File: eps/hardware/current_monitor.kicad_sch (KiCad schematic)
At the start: 23 parts, among them Q5 IRLML0030, Q6 IRLML0030, U5 NCS214RSQT2G, U6 74LVC1G07SE-7

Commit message: start footprint assignment
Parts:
- C22, C23, C24, C25, C26, C27, C28, C29: footprint (none) -> Capacitor_SMD:C_0603_1608Metric
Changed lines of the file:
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@@
 			)
 		)
-		(property "Footprint" ""
+		(property "Footprint" "Capacitor_SMD:C_0603_1608Metric"
 			(at 261.62 58.42 0)
 			(effects
@@
 			)
 		)
-		(property "Footprint" ""
+		(property "Footprint" "Capacitor_SMD:C_0603_1608Metric"
 			(at 127 100.33 0)
 			(effects
@@
 			)
 		)
-		(property "Footprint" ""
+		(property "Footprint" "Capacitor_SMD:C_0603_1608Metric"
 			(at 208.28 58.42 0)
 			(effects
@@
 			)
 		)
-		(property "Footprint" ""
+		(property "Footprint" "Capacitor_SMD:C_0603_1608Metric"
 			(at 106.68 59.69 0)
 			(effects
@@
 			)
 		)
-		(property "Footprint" ""
+		(property "Footprint" "Capacitor_SMD:C_0603_1608Metric"
 			(at 157.48 135.89 0)
 			(effects
@@
 			)
 		)
-		(property "Footprint" ""
+		(property "Footprint" "Capacitor_SMD:C_0603_1608Metric"
 			(at 38.1 123.19 0)
 			(effects
@@
 			)
 		)
-		(property "Footprint" ""
+		(property "Footprint" "Capacitor_SMD:C_0603_1608Metric"
 			(at 102.87 135.89 0)
 			(effects
@@
 			)
 		)
-		(property "Footprint" ""
+		(property "Footprint" "Capacitor_SMD:C_0603_1608Metric"
 			(at 250.19 69.85 0)
 			(effects

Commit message: finish footprint assignment and board setup
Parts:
- NT1: footprint (none) -> NetTie:NetTie-2_SMD_Pad0.5mm
- R24, R25, R26, R27, R28, R29, R30, R31: footprint (none) -> Resistor_SMD:R_0603_1608Metric
- U5: footprint (none) -> Package_TO_SOT_SMD:SOT-363_SC-70-6
- U6: footprint (none) -> Package_TO_SOT_SMD:SOT-353_SC-70-5
- U7: footprint (none) -> Package_TO_SOT_SMD:SOT-23-6
- U8: footprint (none) -> Package_SON:WSON-6-1EP_2x2mm_P0.65mm_EP1x1.6mm
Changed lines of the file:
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@@
 			)
 		)
-		(property "Footprint" ""
+		(property "Footprint" "Resistor_SMD:R_0603_1608Metric"
 			(at 49.276 52.324 90)
 			(effects
@@
 			)
 		)
-		(property "Footprint" ""
+		(property "Footprint" "Resistor_SMD:R_0603_1608Metric"
 			(at 176.276 67.564 90)
 			(effects
@@
 			)
 		)
-		(property "Footprint" ""
+		(property "Footprint" "Resistor_SMD:R_0603_1608Metric"
 			(at 255.016 45.974 90)
 			(effects
@@
 			)
 		)
-		(property "Footprint" ""
+		(property "Footprint" "Package_TO_SOT_SMD:SOT-353_SC-70-5"
 			(at 91.44 73.66 0)
 			(effects
@@
 			)
 		)
-		(property "Footprint" ""
+		(property "Footprint" "Package_SON:WSON-6-1EP_2x2mm_P0.65mm_EP1x1.6mm"
 			(at 232.41 55.88 0)
 			(effects
@@
 			)
 		)
-		(property "Footprint" ""
+		(property "Footprint" "Package_TO_SOT_SMD:SOT-363_SC-70-6"
 			(at 71.12 118.11 0)
 			(effects
@@
 			)
 		)
-		(property "Footprint" ""
+		(property "Footprint" "Resistor_SMD:R_0603_1608Metric"
 			(at 194.056 67.564 90)
 			(effects
@@
 			)
 		)
-		(property "Footprint" ""
+		(property "Footprint" "Resistor_SMD:R_0603_1608Metric"
 			(at 117.856 136.144 90)
 			(effects
@@
 			)
 		)
-		(property "Footprint" ""
+		(property "Footprint" "Resistor_SMD:R_0603_1608Metric"
 			(at 163.576 67.564 90)
 			(effects
@@
 			)
 		)
-		(property "Footprint" ""
+		(property "Footprint" "NetTie:NetTie-2_SMD_Pad0.5mm"
 			(at 57.15 41.91 0)
 			(effects
@@
 			)
 		)
-		(property "Footprint" ""
+		(property "Footprint" "Resistor_SMD:R_0603_1608Metric"
 			(at 213.106 33.274 90)
 			(effects
@@
 			)
 		)
-		(property "Footprint" ""
+		(property "Footprint" "Package_TO_SOT_SMD:SOT-23-6"
 			(at 139.7 116.84 0)
 			(effects
@@
 			)
 		)
-		(property "Footprint" ""
+		(property "Footprint" "Resistor_SMD:R_0603_1608Metric"
 			(at 250.444 91.694 90)
 			(effects

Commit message: fix update errors
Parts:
- U8: value ~ -> TPS22810DRVT
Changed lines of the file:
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@@
 			)
 		)
-		(property "Value" "~"
+		(property "Value" "TPS22810DRVT"
 			(at 232.41 38.1 0)
 			(effects
@@
 		(pin "2"
 		)
+		(pin "7"
+		)
 		(instances

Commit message: schematic fixes
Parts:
- C22, C23, C24, C25, C26, C27, C28, C29: footprint Capacitor_SMD:C_0603_1608Metric -> Capacitor_SMD:C_0402_1005Metric
- R24, R25, R26, R27, R28, R29, R30, R31: footprint Resistor_SMD:R_0603_1608Metric -> Resistor_SMD:R_0402_1005Metric
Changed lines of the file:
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@@
 			)
 		)
-		(property "Footprint" "Resistor_SMD:R_0603_1608Metric"
+		(property "Footprint" "Resistor_SMD:R_0402_1005Metric"
 			(at 49.276 52.324 90)
 			(effects
@@
 			)
 		)
-		(property "Footprint" "Resistor_SMD:R_0603_1608Metric"
+		(property "Footprint" "Resistor_SMD:R_0402_1005Metric"
 			(at 176.276 67.564 90)
 			(effects
@@
 			)
 		)
-		(property "Footprint" "Capacitor_SMD:C_0603_1608Metric"
+		(property "Footprint" "Capacitor_SMD:C_0402_1005Metric"
 			(at 261.62 58.42 0)
 			(effects
@@
 			)
 		)
-		(property "Footprint" "Capacitor_SMD:C_0603_1608Metric"
+		(property "Footprint" "Capacitor_SMD:C_0402_1005Metric"
 			(at 127 100.33 0)
 			(effects
@@
 			)
 		)
-		(property "Footprint" "Resistor_SMD:R_0603_1608Metric"
+		(property "Footprint" "Resistor_SMD:R_0402_1005Metric"
 			(at 255.016 45.974 90)
 			(effects
@@
 			)
 		)
-		(property "Footprint" "Capacitor_SMD:C_0603_1608Metric"
+		(property "Footprint" "Capacitor_SMD:C_0402_1005Metric"
 			(at 208.28 58.42 0)
 			(effects
@@
 			)
 		)
-		(property "Footprint" "Capacitor_SMD:C_0603_1608Metric"
+		(property "Footprint" "Capacitor_SMD:C_0402_1005Metric"
 			(at 106.68 59.69 0)
 			(effects
@@
 			)
 		)
-		(property "Footprint" "Resistor_SMD:R_0603_1608Metric"
+		(property "Footprint" "Resistor_SMD:R_0402_1005Metric"
 			(at 194.056 67.564 90)
 			(effects
@@
 			)
 		)
-		(property "Footprint" "Resistor_SMD:R_0603_1608Metric"
+		(property "Footprint" "Resistor_SMD:R_0402_1005Metric"
 			(at 117.856 136.144 90)
 			(effects
@@
 			)
 		)
-		(property "Footprint" "Resistor_SMD:R_0603_1608Metric"
+		(property "Footprint" "Resistor_SMD:R_0402_1005Metric"
 			(at 163.576 67.564 90)
 			(effects
@@
 			)
 		)
-		(property "Footprint" "Capacitor_SMD:C_0603_1608Metric"
+		(property "Footprint" "Capacitor_SMD:C_0402_1005Metric"
 			(at 157.48 135.89 0)
 			(effects
@@
 			)
 		)
-		(property "Footprint" "Capacitor_SMD:C_0603_1608Metric"
+		(property "Footprint" "Capacitor_SMD:C_0402_1005Metric"
 			(at 38.1 123.19 0)
 			(effects
@@
 			)
 		)
-		(property "Footprint" "Capacitor_SMD:C_0603_1608Metric"
+		(property "Footprint" "Capacitor_SMD:C_0402_1005Metric"
 			(at 102.87 135.89 0)
 			(effects
@@
 			)
 		)
-		(property "Footprint" "Capacitor_SMD:C_0603_1608Metric"
+		(property "Footprint" "Capacitor_SMD:C_0402_1005Metric"
 			(at 250.19 69.85 0)
 			(effects
@@
 			)
 		)
-		(property "Footprint" "Resistor_SMD:R_0603_1608Metric"
+		(property "Footprint" "Resistor_SMD:R_0402_1005Metric"
 			(at 213.106 33.274 90)
 			(effects
@@
 			)
 		)
-		(property "Footprint" "Resistor_SMD:R_0603_1608Metric"
+		(property "Footprint" "Resistor_SMD:R_0402_1005Metric"
 			(at 250.444 91.694 90)
 			(effects

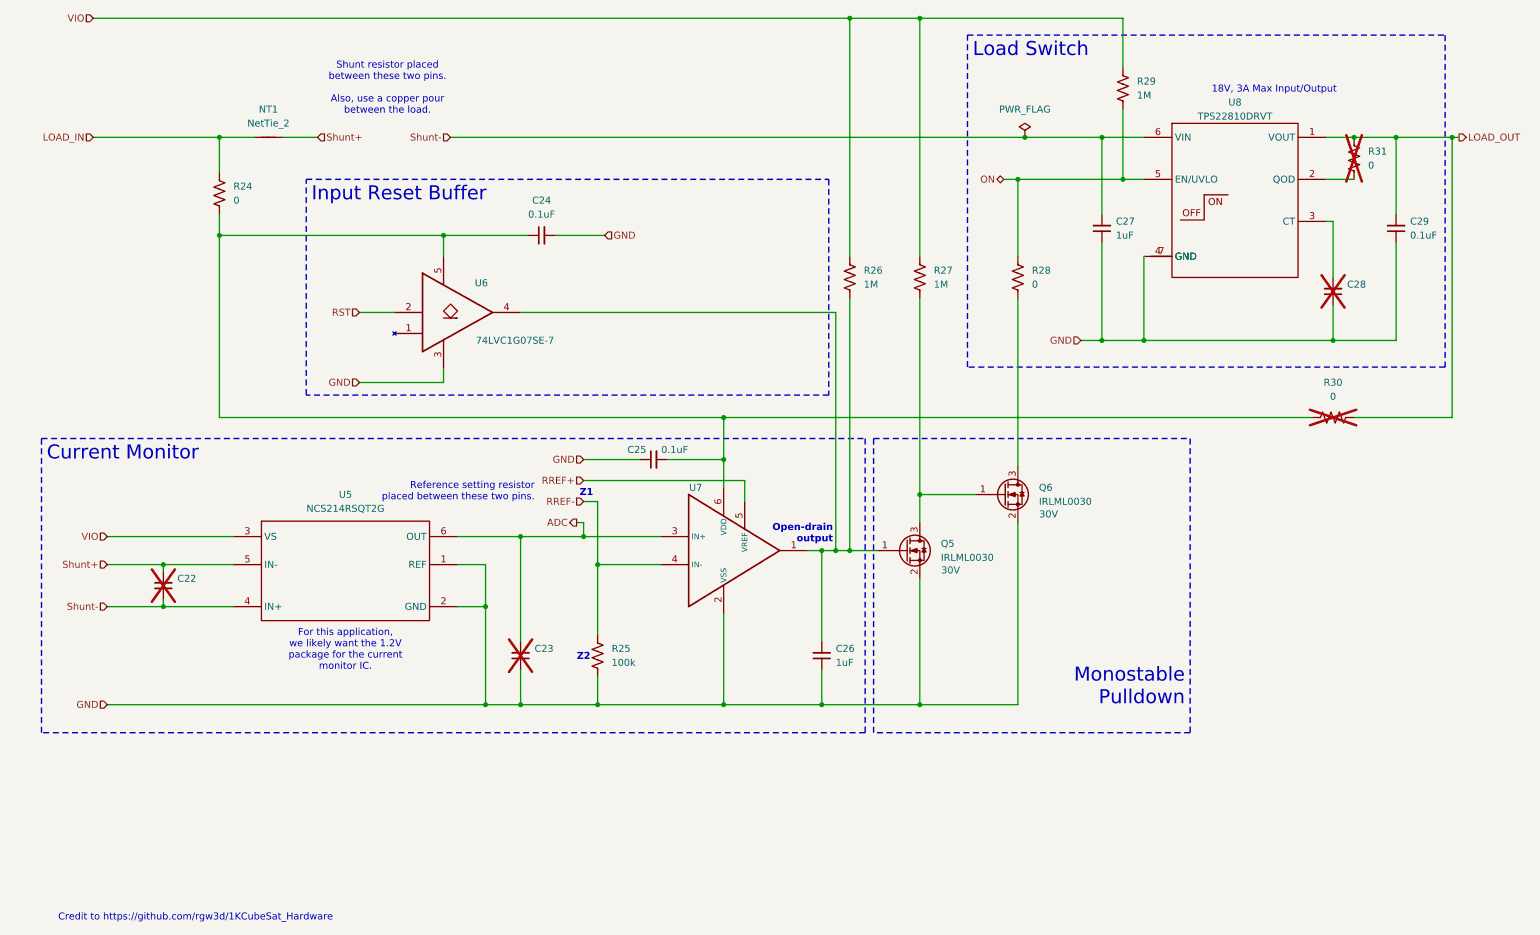
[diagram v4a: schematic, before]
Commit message: start placement of one current monitor
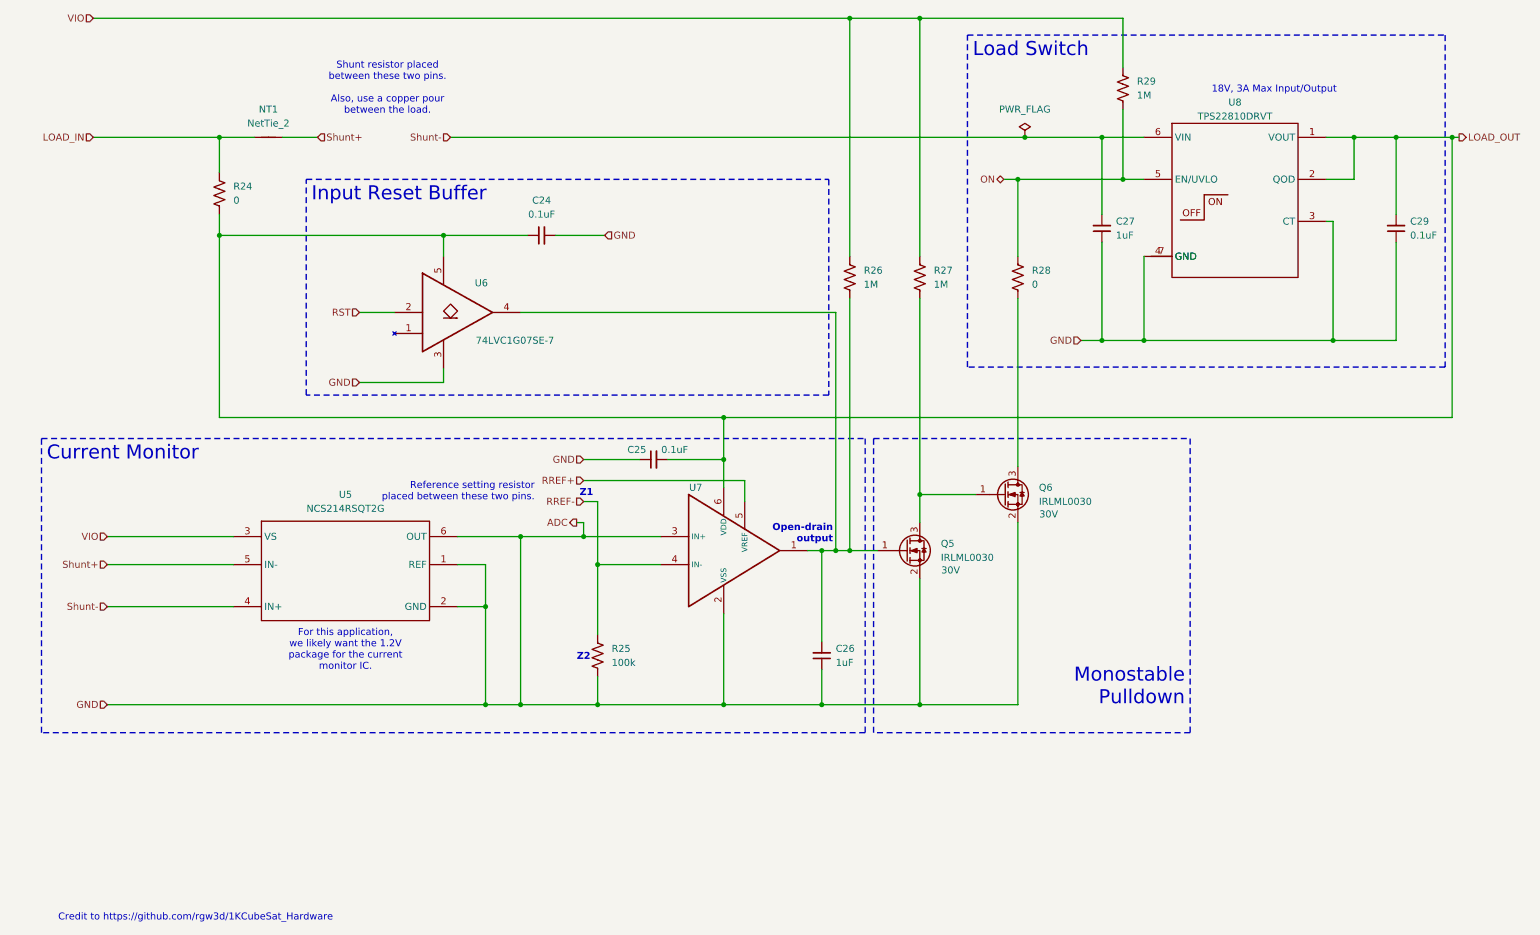
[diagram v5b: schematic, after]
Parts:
- removed C22, C23, C28: ~, Capacitor_SMD:C_0402_1005Metric, symbol Device:C_Small
- removed R30, R31: 0, Resistor_SMD:R_0402_1005Metric, symbol Device:R_US
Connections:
- net GND is gone; now on net ADC: C24.2, C25.1, C26.1, C27.1, C29.1, Q5.2 (S), Q6.2 (S), R25.2, U5.1 (REF), U5.2 (GND), U6.3, U7.2 (VSS), U8.4 (GND)
- net ADC: now also U8.3 (CT)
- net LOAD_OUT: now also C24.1, C25.2, R24.2, U6.5, U7.6 (VDD), U8.2 (QOD)

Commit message: add better current monitoring layout
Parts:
- C27: footprint Capacitor_SMD:C_0402_1005Metric -> Capacitor_SMD:C_0805_2012Metric
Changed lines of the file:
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@@
 			)
 		)
-		(property "Footprint" "Capacitor_SMD:C_0402_1005Metric"
+		(property "Footprint" "Capacitor_SMD:C_0805_2012Metric"
 			(at 208.28 58.42 0)
 			(effects

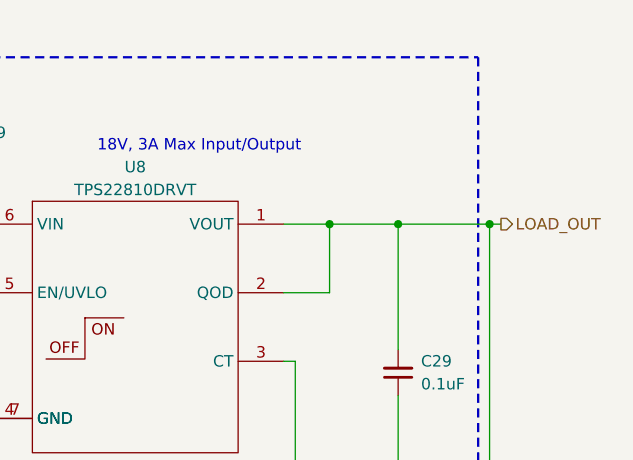
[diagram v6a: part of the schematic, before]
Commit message: finish component placement
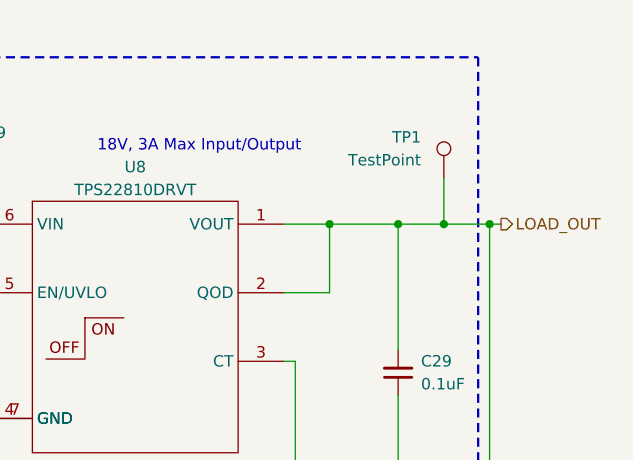
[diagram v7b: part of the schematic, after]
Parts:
- added TP1: TestPoint, TestPoint:TestPoint_Pad_D1.0mm, symbol Connector:TestPoint
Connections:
- net LOAD_OUT: now also TP1.1
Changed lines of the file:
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@@
 	)
 	(junction
+		(at 266.7 41.91)
+		(diameter 0)
+		(color 0 0 0 0)
+	)
+	(junction
 		(at 162.56 116.84)
 		(diameter 0)
@@
 	(wire
 		(pts
+			(xy 266.7 41.91) (xy 271.78 41.91)
+		)
+		(stroke
+			(width 0)
+			(type default)
+		)
+	)
+	(wire
+		(pts
 			(xy 114.3 107.95) (xy 116.84 107.95)
 		)
@@
 	(wire
 		(pts
+			(xy 266.7 36.83) (xy 266.7 41.91)
+		)
+		(stroke
+			(width 0)
+			(type default)
+		)
+	)
+	(wire
+		(pts
 			(xy 175.26 121.92) (xy 175.26 144.78)
 		)
@@
 	(wire
 		(pts
-			(xy 261.62 41.91) (xy 271.78 41.91)
+			(xy 261.62 41.91) (xy 266.7 41.91)
 		)
 		(stroke
@@
 					(unit 1)
 				)
+			)
+		)
+	)
+	(symbol
+		(lib_id "Connector:TestPoint")
+		(at 266.7 36.83 0)
+		(unit 1)
+		(exclude_from_sim no)
+		(in_bom yes)
+		(on_board yes)
+		(dnp no)
+		(property "Reference" "TP1"
+			(at 264.16 32.2579 0)
+			(effects
+				(font
+					(size 1.27 1.27)
+				)
+				(justify right)
+			)
+		)
+		(property "Value" "TestPoint"
+			(at 264.16 34.7979 0)
+			(effects
+				(font
+					(size 1.27 1.27)
+				)
+				(justify right)
+			)
+		)
+		(property "Footprint" "TestPoint:TestPoint_Pad_D1.0mm"
+			(at 271.78 36.83 0)
+			(effects
+				(font
+					(size 1.27 1.27)
+				)
+				(hide yes)
+			)
+		)
+		(property "Datasheet" "~"
+			(at 271.78 36.83 0)
+			(effects
+				(font
+					(size 1.27 1.27)
+				)
+				(hide yes)
+			)
+		)
+		(property "Description" "test point"
+			(at 266.7 36.83 0)
+			(effects
+				(font
+					(size 1.27 1.27)
+				)
+				(hide yes)
+			)
+		)
+		(pin "1"
+		)
+		(instances
+			(project ""
+				(path "/9e0ae2e7-d4be-41b4-8312-0d2aceea2180/373e68a1-9d85-40af-a211-fd16b724d579/147083ce-7ff1-4330-8f9d-90a49a4fc524"
+					(reference "TP1")
+					(unit 1)
+				)
+				(path "/9e0ae2e7-d4be-41b4-8312-0d2aceea2180/373e68a1-9d85-40af-a211-fd16b724d579/2d75be79-5fbf-443b-b5d5-5d4b69bafd44"
+					(reference "TP6")
+					(unit 1)
+				)
+				(path "/9e0ae2e7-d4be-41b4-8312-0d2aceea2180/373e68a1-9d85-40af-a211-fd16b724d579/5cad98b7-3bab-409d-b3cc-44c7c987247d"
+					(reference "TP8")
+					(unit 1)
+				)
+				(path "/9e0ae2e7-d4be-41b4-8312-0d2aceea2180/373e68a1-9d85-40af-a211-fd16b724d579/6395c9e8-c5c2-425c-900f-887032a0fcd5"
+					(reference "TP7")
+					(unit 1)
+				)
+				(path "/9e0ae2e7-d4be-41b4-8312-0d2aceea2180/373e68a1-9d85-40af-a211-fd16b724d579/872f2c00-0abb-4b4b-8247-47a38a86d037"
+					(reference "TP4")
+					(unit 1)
+				)
+				(path "/9e0ae2e7-d4be-41b4-8312-0d2aceea2180/373e68a1-9d85-40af-a211-fd16b724d579/8d850b09-e8c3-4e43-ac4b-0b319f56a96e"
+					(reference "TP2")
+					(unit 1)
+				)
+				(path "/9e0ae2e7-d4be-41b4-8312-0d2aceea2180/373e68a1-9d85-40af-a211-fd16b724d579/d546f4db-215e-434b-a7ba-86417010bf75"
+					(reference "TP5")
+					(unit 1)
+				)
+				(path "/9e0ae2e7-d4be-41b4-8312-0d2aceea2180/373e68a1-9d85-40af-a211-fd16b724d579/fe512522-4dcc-4302-acc3-dfd05772ec49"
+					(reference "TP3")
+					(unit 1)
+				)

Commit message: continue routing
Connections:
- net ADC: now also U8.7 (GND)
- net LOAD_OUT: no longer C24.1, C25.2, R24.2, U6.5, U7.6 (VDD)
- new net: C24.1, C25.2, R24.2, U6.5, U7.6 (VDD)
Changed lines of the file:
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@@
-	)
-	(junction
-		(at 139.7 92.71)
-		(diameter 0)
-		(color 0 0 0 0)
-	)
-	(junction
-		(at 271.78 41.91)
-		(diameter 0)
-		(color 0 0 0 0)
 	)
 	(junction
@@
 	(wire
 		(pts
-			(xy 271.78 92.71) (xy 271.78 41.91)
-		)
-		(stroke
-			(width 0)
-			(type default)
-		)
-	)
-	(wire
-		(pts
 			(xy 157.48 144.78) (xy 175.26 144.78)
 		)
@@
 	(wire
 		(pts
-			(xy 266.7 41.91) (xy 271.78 41.91)
+			(xy 266.7 41.91) (xy 273.05 41.91)
 		)
 		(stroke
@@
 	(wire
 		(pts
-			(xy 139.7 92.71) (xy 271.78 92.71)
-		)
-		(stroke
-			(width 0)
-			(type default)
-		)
-	)
-	(wire
-		(pts
 			(xy 160.02 116.84) (xy 162.56 116.84)
 		)
@@
 		)
 		(stroke
-			(width 0)
-			(type default)
-		)
-	)
-	(wire
-		(pts
-			(xy 271.78 41.91) (xy 273.05 41.91)
-		)
-		(stroke
